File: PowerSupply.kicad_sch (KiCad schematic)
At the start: 58 parts, among them U1 MT3420C-mt3420c, U2 MT3420C-mt3420c, U3 MT3420C-mt3420c, U4 X1000

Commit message: Update (Display)
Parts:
- R1, R2, R3, R4, R5, R6, R7, R8, R9: footprint (none) -> Resistor_SMD:R_0402_1005Metric
- U4: footprint (none) -> TheBrutzlers_Lib:BGA256C80P16X16_1300X1300X130N
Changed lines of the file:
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@@
       (effects (font (size 1.27 1.27)) (justify left))
     )
-    (property "Footprint" "" (id 2) (at 121.412 107.95 90)
+    (property "Footprint" "Resistor_SMD:R_0402_1005Metric" (id 2) (at 121.412 107.95 90)
       (effects (font (size 1.27 1.27)) hide)
     )
@@
     (property "Reference" "R1" (id 0) (at 58.42 43.18 90))
     (property "Value" "50K" (id 1) (at 58.42 40.64 90))
-    (property "Footprint" "" (id 2) (at 58.42 42.418 90)
+    (property "Footprint" "Resistor_SMD:R_0402_1005Metric" (id 2) (at 58.42 42.418 90)
       (effects (font (size 1.27 1.27)) hide)
     )
@@
       (effects (font (size 1.27 1.27)) (justify left))
     )
-    (property "Footprint" "" (id 2) (at 121.412 35.56 90)
+    (property "Footprint" "Resistor_SMD:R_0402_1005Metric" (id 2) (at 121.412 35.56 90)
       (effects (font (size 1.27 1.27)) hide)
     )
@@
       (effects (font (size 1.27 1.27)) (justify left))
     )
-    (property "Footprint" "" (id 2) (at 121.412 66.04 90)
+    (property "Footprint" "Resistor_SMD:R_0402_1005Metric" (id 2) (at 121.412 66.04 90)
       (effects (font (size 1.27 1.27)) hide)
     )
@@
       (effects (font (size 1.27 1.27)) (justify left))
     )
-    (property "Footprint" "" (id 2) (at 121.412 76.2 90)
+    (property "Footprint" "Resistor_SMD:R_0402_1005Metric" (id 2) (at 121.412 76.2 90)
       (effects (font (size 1.27 1.27)) hide)
     )
@@
       (effects (font (size 1.27 1.27)) (justify left))
     )
-    (property "Footprint" "" (id 2) (at 130.302 66.04 90)
+    (property "Footprint" "Resistor_SMD:R_0402_1005Metric" (id 2) (at 130.302 66.04 90)
       (effects (font (size 1.27 1.27)) hide)
     )
@@
     (property "Reference" "U4" (id 0) (at 210.82 93.98 0))
     (property "Value" "X1000" (id 1) (at 210.82 96.52 0))
-    (property "Footprint" "" (id 2) (at 205.74 111.76 0)
+    (property "Footprint" "TheBrutzlers_Lib:BGA256C80P16X16_1300X1300X130N" (id 2) (at 205.74 111.76 0)
       (effects (font (size 1.27 1.27)) (justify left) hide)
     )
@@
     (property "Reference" "R2" (id 0) (at 62.23 105.41 90))
     (property "Value" "30K" (id 1) (at 62.23 102.87 90))
-    (property "Footprint" "" (id 2) (at 62.23 104.648 90)
+    (property "Footprint" "Resistor_SMD:R_0402_1005Metric" (id 2) (at 62.23 104.648 90)
       (effects (font (size 1.27 1.27)) hide)
     )
@@
       (effects (font (size 1.27 1.27)) (justify left))
     )
-    (property "Footprint" "" (id 2) (at 121.412 97.79 90)
+    (property "Footprint" "Resistor_SMD:R_0402_1005Metric" (id 2) (at 121.412 97.79 90)
       (effects (font (size 1.27 1.27)) hide)
     )
@@
       (effects (font (size 1.27 1.27)) (justify left))
     )
-    (property "Footprint" "" (id 2) (at 121.412 45.72 90)
-      (effects (font (size 1.27 1.27)) hide)
-    )
+    (property "Footprint" "Resistor_SMD:R_0402_1005Metric" (id 2) (at 121.412 45.72 90)
+      (effects (font (size 1.27 1.27)) hide)
+    )

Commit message: Add Audio
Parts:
- U1, U2, U3: LCSC (none) -> C181741; Number C181741 -> (none)
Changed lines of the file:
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@@
       (effects (font (size 1.27 1.27)) hide)
     )
-    (property "Number" "C181741" (id 4) (at 92.71 38.1 0)
+    (property "Number" "" (id 4) (at 92.71 38.1 0)
+      (effects (font (size 1.27 1.27)) hide)
+    )
+    (property "LCSC" "C181741" (id 5) (at 92.71 38.1 0)
       (effects (font (size 1.27 1.27)) hide)
     )
@@
       (effects (font (size 1.27 1.27)) hide)
     )
-    (property "Number" "C181741" (id 4) (at 92.71 100.33 0)
+    (property "Number" "" (id 4) (at 92.71 100.33 0)
+      (effects (font (size 1.27 1.27)) hide)
+    )
+    (property "LCSC" "C181741" (id 5) (at 92.71 100.33 0)
       (effects (font (size 1.27 1.27)) hide)
     )
@@
       (effects (font (size 1.27 1.27)) hide)
     )
-    (property "Number" "C181741" (id 4) (at 92.71 68.58 0)
-      (effects (font (size 1.27 1.27)) hide)
-    )
+    (property "Number" "" (id 4) (at 92.71 68.58 0)
+      (effects (font (size 1.27 1.27)) hide)
+    )
+    (property "LCSC" "C181741" (id 5) (at 92.71 68.58 0)
+      (effects (font (size 1.27 1.27)) hide)
+    )

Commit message: New i.mx6 Version
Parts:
- removed C10, C11, C12, C13, C14, C15, C16, C17, C18, C19, C20, C21, C22, C23, C24, C25, C26, C27, C28, C29, C30, C31, C32, C33, C34, C35, C36, C37, C38, C39, C9: 100n, Capacitor_SMD:C_0402_1005Metric, symbol Device:C
- removed R10: 240, symbol Device:R
- removed U4: X1000, TheBrutzlers_Lib:BGA256C80P16X16_1300X1300X130N, symbol TheBrutzlers_Lib:X1000
- added C? (x6): 100n, Capacitor_SMD:C_0402_1005Metric, symbol Device:C
- added C?: 22µ, Capacitor_SMD:C_0603_1608Metric, symbol Device:C
- added U? (x2): IMX6UL, TheBrutzlers_Lib:IMX6UL_BGA289, symbol TheBrutzlers_Lib:IMX6UL
- R5: value 200K -> 133K
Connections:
- net +5V: now also U2.1 (EN)
- net GND: now also C?.1, C?.1, C?.1, C?.1, C?.1, C?.2, C?.2, U?.A1 (VSS), U?.A17 (VSS), U?.C11 (VSS), U?.C15 (VSS), U?.C3 (VSS), U?.C7 (VSS), U?.E11 (VSS), U?.E8 (VSS), U?.F10 (VSS), U?.F11 (VSS), U?.F12 (VSS), U?.F6 (VSS), U?.F7 (VSS), U?.F8 (VSS), U?.F9 (VSS), U?.G12 (VSS), U?.G15 (VSS), U?.G3 (VSS), U?.G5 (VSS), U?.G7 (VSS), U?.H12 (VSS), U?.H7 (VSS), U?.J12 (VSS), U?.J5 (VSS), U?.J7 (VSS), U?.K12 (VSS), U?.K7 (VSS), U?.L12 (VSS), U?.L3 (VSS), U?.L7 (VSS), U?.M10 (VSS), U?.M11 (VSS), U?.M12 (NGND_KEL0), U?.M7 (VSS), U?.M8 (VSS), U?.M9 (VSS), U?.N3 (VSS), U?.N5 (VSS), U?.R11 (VSS), U?.R16 (VSS), U?.R17 (VSS), U?.R3 (VSS), U?.R5 (VSS), U?.R7 (VSS), U?.T14 (VSS), U?.U1 (VSS), U?.U14 (VSS), U?.U17 (VSS)
- net +1V8 renamed +1V4
- new net: C?.1, C?.1, C?.2, C?.2, C?.2, C?.2, C?.2, U?.H10 (VDD_SOC_IN), U?.H9 (VDD_SOC_IN), U?.J10 (VDD_SOC_IN), U?.J9 (VDD_SOC_IN), U?.K10 (VDD_SOC_IN), U?.K9 (VDD_SOC_IN)

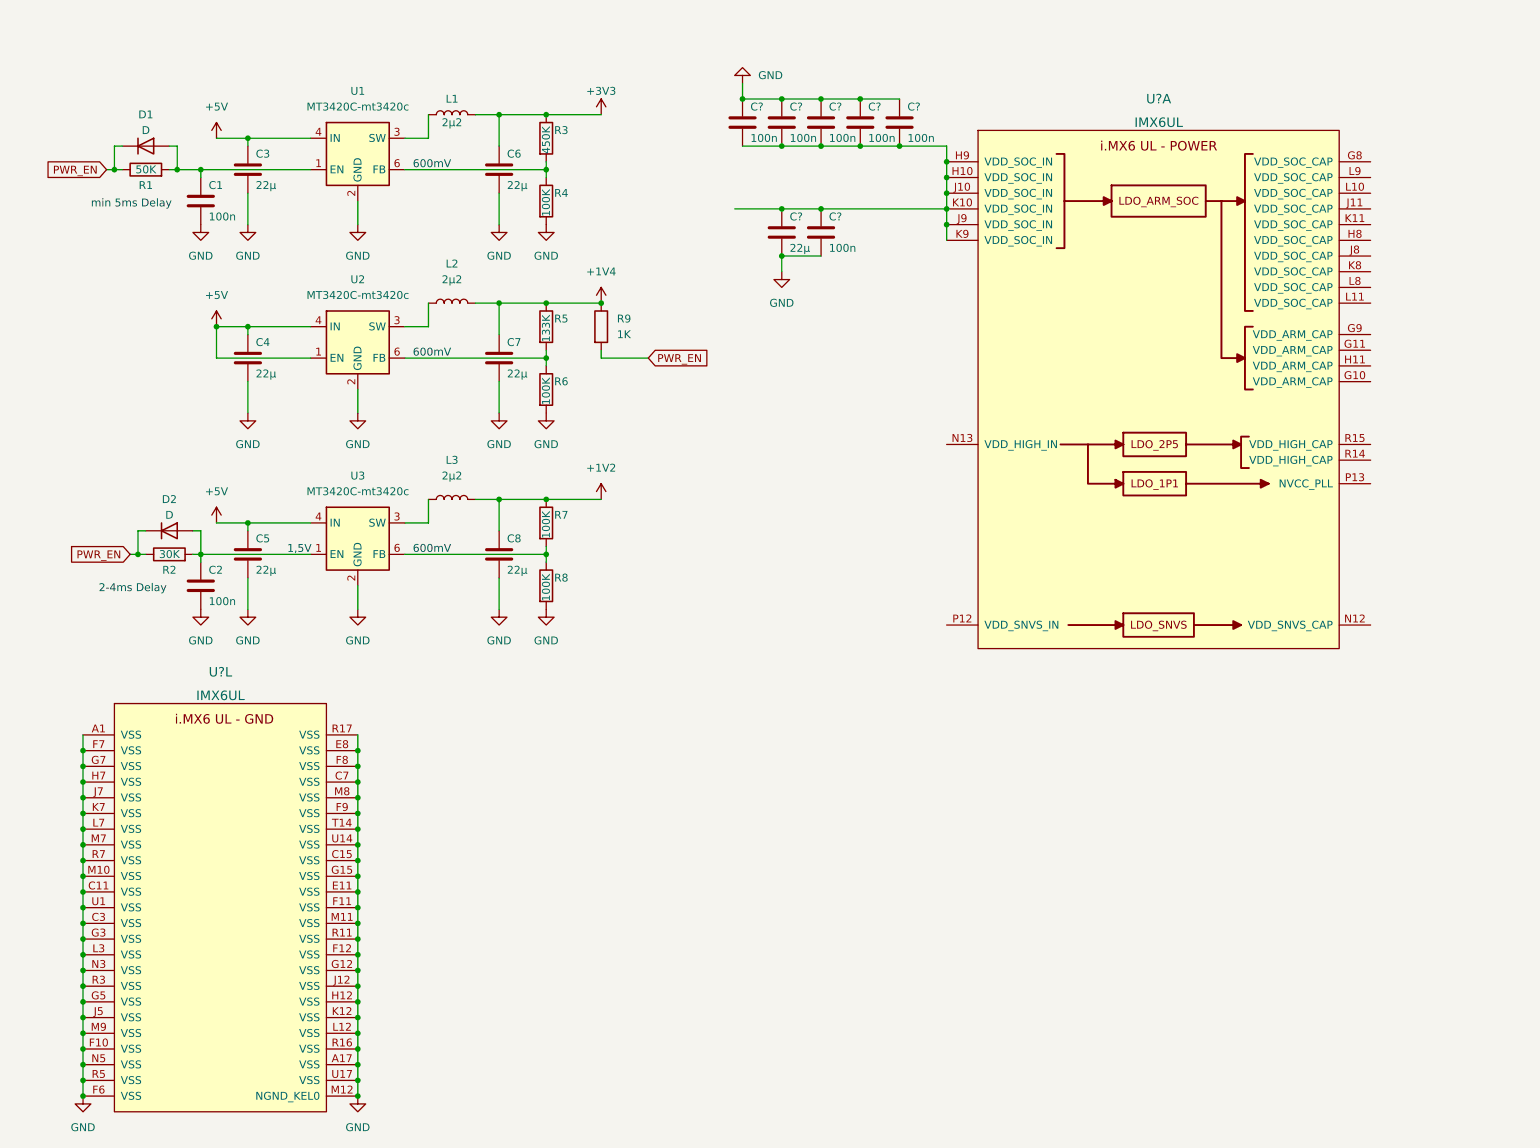
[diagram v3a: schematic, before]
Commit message: Display Update
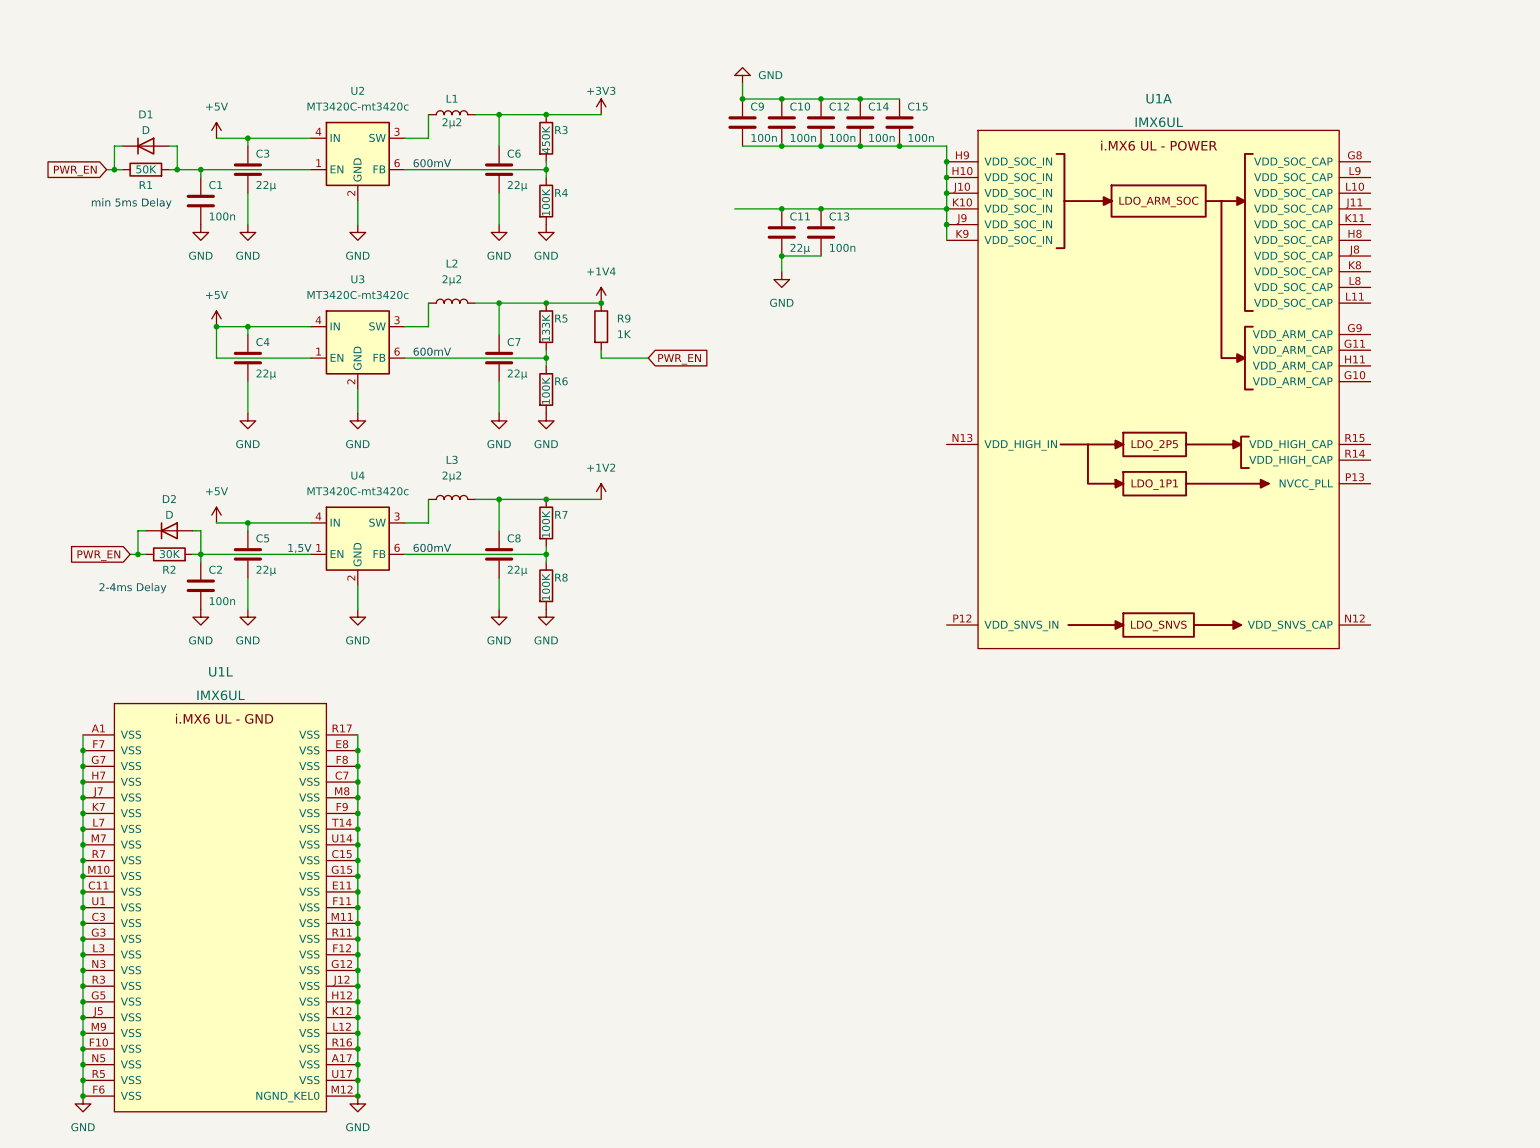
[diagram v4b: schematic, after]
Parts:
- gave numbers to parts that had none: 8
- renumbered U1 to U2, U2 to U3, U3 to U4

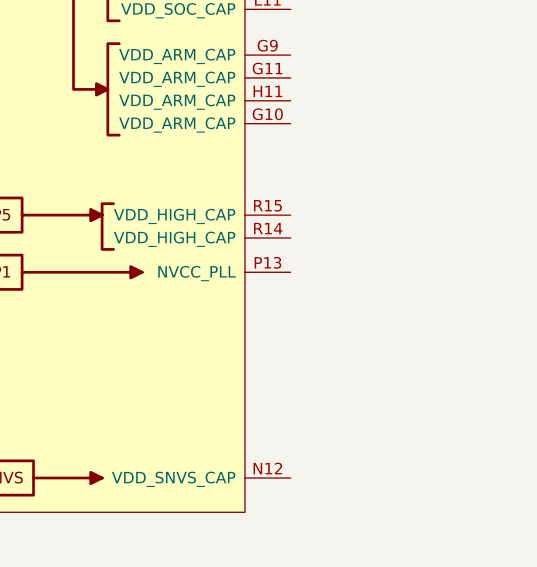
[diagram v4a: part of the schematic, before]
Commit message: update DDR
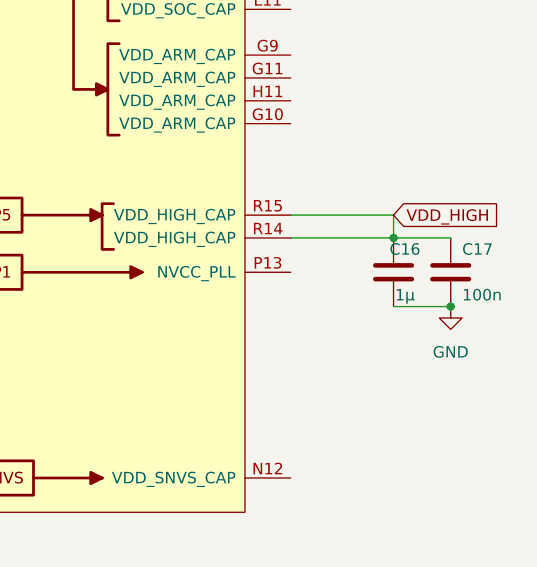
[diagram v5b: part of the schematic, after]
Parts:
- added C16: 1µ, Capacitor_SMD:C_0402_1005Metric, symbol Device:C
- added C17: 100n, Capacitor_SMD:C_0402_1005Metric, symbol Device:C
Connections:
- net GND: now also C16.1, C17.2
- net VDD_HIGH: now reaches U1.R14 (VDD_HIGH_CAP)
- net VDD_HIGH: now also U1.R15 (VDD_HIGH_CAP), C16.2, C17.1
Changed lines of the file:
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@@
   (junction (at 48.26 142.24) (diameter 0) (color 0 0 0 0)
   )
+  (junction (at 267.97 87.63) (diameter 0) (color 0 0 0 0)
+  )
   (junction (at 161.29 36.83) (diameter 0) (color 0 0 0 0)
   )
@@
   (junction (at 92.71 170.18) (diameter 0) (color 0 0 0 0)
   )
+  (junction (at 274.32 95.25) (diameter 0) (color 0 0 0 0)
+  )
   (junction (at 48.26 170.18) (diameter 0) (color 0 0 0 0)
   )
@@
     (stroke (width 0) (type default) (color 0 0 0 0))
   )
+  (wire (pts (xy 256.54 87.63) (xy 267.97 87.63))
+    (stroke (width 0) (type default) (color 0 0 0 0))
+  )
   (wire (pts (xy 123.19 69.85) (xy 123.19 71.12))
     (stroke (width 0) (type default) (color 0 0 0 0))
@@
     (stroke (width 0) (type default) (color 0 0 0 0))
   )
+  (wire (pts (xy 267.97 87.63) (xy 274.32 87.63))
+    (stroke (width 0) (type default) (color 0 0 0 0))
+  )
   (wire (pts (xy 69.85 71.12) (xy 69.85 66.04))
     (stroke (width 0) (type default) (color 0 0 0 0))
@@
     (stroke (width 0) (type default) (color 0 0 0 0))
   )
+  (wire (pts (xy 267.97 95.25) (xy 274.32 95.25))
+    (stroke (width 0) (type default) (color 0 0 0 0))
+  )
   (wire (pts (xy 48.26 144.78) (xy 48.26 147.32))
     (stroke (width 0) (type default) (color 0 0 0 0))
@@
     (stroke (width 0) (type default) (color 0 0 0 0))
   )
+  (wire (pts (xy 267.97 85.09) (xy 267.97 87.63))
+    (stroke (width 0) (type default) (color 0 0 0 0))
+  )
   (wire (pts (xy 48.26 187.96) (xy 48.26 190.5))
     (stroke (width 0) (type default) (color 0 0 0 0))
@@
   )
   (wire (pts (xy 92.71 165.1) (xy 92.71 167.64))
+    (stroke (width 0) (type default) (color 0 0 0 0))
+  )
+  (wire (pts (xy 256.54 85.09) (xy 267.97 85.09))
     (stroke (width 0) (type default) (color 0 0 0 0))
   )
@@
   (text "600mV" (at 101.6 71.12 0)
     (effects (font (size 1.27 1.27)) (justify left bottom))
+  )
+  (global_label "VDD_HIGH" (shape input) (at 267.97 85.09 0) (fields_autoplaced)
+    (effects (font (size 1.27 1.27)) (justify left))
+    (property "Intersheet References" "${INTERSHEET_REFS}" (id 0) (at 279.515 85.0106 0)
+      (effects (font (size 1.27 1.27)) (justify left) hide)
+    )
   )
   (global_label "PWR_EN" (shape input) (at 139.7 71.12 0) (fields_autoplaced)
@@
     )
     (pin "1")
+  )
+  (symbol (lib_id "Device:C") (at 274.32 91.44 0) (unit 1)
+    (in_bom yes) (on_board yes)
+    (property "Reference" "C17" (id 0) (at 275.59 88.9 0)
+      (effects (font (size 1.27 1.27)) (justify left))
+    )
+    (property "Value" "100n" (id 1) (at 275.59 93.98 0)
+      (effects (font (size 1.27 1.27)) (justify left))
+    )
+    (property "Footprint" "Capacitor_SMD:C_0402_1005Metric" (id 2) (at 275.2852 95.25 0)
+      (effects (font (size 1.27 1.27)) hide)
+    )
+    (property "Datasheet" "~" (id 3) (at 274.32 91.44 0)
+      (effects (font (size 1.27 1.27)) hide)
+    )
+    (property "LCSC" "C83056" (id 4) (at 274.32 91.44 0)
+      (effects (font (size 1.27 1.27)) hide)
+    )
+    (pin "1")
+    (pin "2")
   )
   (symbol (lib_id "Device:R") (at 123.19 76.2 0) (unit 1)
@@
     (pin "1")
   )
+  (symbol (lib_id "Device:C") (at 267.97 91.44 180) (unit 1)
+    (in_bom yes) (on_board yes)
+    (property "Reference" "C16" (id 0) (at 269.24 88.9 0))
+    (property "Value" "1µ" (id 1) (at 269.24 93.98 0))
+    (property "Footprint" "Capacitor_SMD:C_0402_1005Metric" (id 2) (at 267.0048 87.63 0)
+      (effects (font (size 1.27 1.27)) hide)
+    )
+    (property "Datasheet" "~" (id 3) (at 267.97 91.44 0)
+      (effects (font (size 1.27 1.27)) hide)
+    )
+    (property "LCSC" "C5142580" (id 4) (at 267.97 91.44 0)
+      (effects (font (size 1.27 1.27)) hide)
+    )
+    (pin "1")
+    (pin "2")
+  )
   (symbol (lib_id "Device:L") (at 107.95 93.98 90) (unit 1)
     (in_bom yes) (on_board yes) (fields_autoplaced)
@@
     (pin "2")
   )
+  (symbol (lib_id "power:GND") (at 274.32 95.25 0) (unit 1)
+    (in_bom yes) (on_board yes) (fields_autoplaced)
+    (property "Reference" "#PWR028" (id 0) (at 274.32 101.6 0)
+      (effects (font (size 1.27 1.27)) hide)
+    )
+    (property "Value" "GND" (id 1) (at 274.32 100.33 0))
+    (property "Footprint" "" (id 2) (at 274.32 95.25 0)
+      (effects (font (size 1.27 1.27)) hide)
+    )
+    (property "Datasheet" "" (id 3) (at 274.32 95.25 0)
+      (effects (font (size 1.27 1.27)) hide)
+    )
+    (pin "1")
+  )
   (symbol (lib_id "power:+5V") (at 69.85 97.79 0) (unit 1)
